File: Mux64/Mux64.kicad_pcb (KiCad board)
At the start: 4 copper layers, 198.3 x 130.3 mm, 143 parts, among them J1 QTE-020-01-X-D-A, J10 Conn_01x24, J11 Screw_Terminal_01x12, J12 Screw_Terminal_01x12, J13 Screw_Terminal_01x12, J14 Screw_Terminal_01x12, J15 Screw_Terminal_01x12, J16 Screw_Terminal_01x12, J17 Screw_Terminal_01x12, J18 Screw_Terminal_01x12, J2 QTE-020-01-X-D-A, J3 QTE-020-01-X-D-A, J4 QTE-020-01-X-D-A, J5 QTE-020-01-X-D-A, J6 QTE-020-01-X-D-A, J7 Conn_01x24, J8 Conn_01x24, J9 Conn_01x24, U1 LD1117AS12TR, U2 MAX6070

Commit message: Add files via upload
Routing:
- net GND: track 511.1 -> 513.4 mm, vias 126 -> 127
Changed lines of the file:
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@@
   (segment (start 216.18 52.43) (end 216.6 52.01) (width 0.1524) (layer "F.Cu") (net 2))
   (segment (start 214.04 50.83) (end 216.6 50.83) (width 0.1524) (layer "F.Cu") (net 2))
+  (segment (start 178.6725 60.92) (end 176.34 60.92) (width 0.25) (layer "F.Cu") (net 2))
   (segment (start 219.23 51.0525) (end 216.6125 51.0525) (width 0.1524) (layer "F.Cu") (net 2))
   (segment (start 237.86 46.83) (end 236.33 46.83) (width 0.1524) (layer "F.Cu") (net 2))
@@
   (via (at 205.27 137.25) (size 0.8) (drill 0.4) (layers "F.Cu" "B.Cu") (net 2))
   (via (at 80.37 44.92) (size 0.8) (drill 0.4) (layers "F.Cu" "B.Cu") (net 2))
+  (via (at 176.34 60.92) (size 0.8) (drill 0.4) (layers "F.Cu" "B.Cu") (net 2))
   (via (at 79.25 95.71) (size 0.8) (drill 0.4) (layers "F.Cu" "B.Cu") (net 2))
   (via (at 79.95 29.65) (size 0.8) (drill 0.4) (layers "F.Cu" "B.Cu") (net 2))

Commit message: Add files via upload
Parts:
- added H1: MountingHole, MountingHole:MountingHole_2.5mm, F.Cu at (250.7, 151.7)
- added H2: MountingHole, MountingHole:MountingHole_2.5mm, F.Cu at (85.0, 151.7)
- added H3: MountingHole, MountingHole:MountingHole_2.5mm, F.Cu at (85.0, 28.4)
- added H4: MountingHole, MountingHole:MountingHole_2.5mm, F.Cu at (250.7, 28.4)
- moved TP1 7.51 mm to (192.3, 46.9)
- moved R8 3.64 mm to (124.2, 99.0)
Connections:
- C1 pad 2: GND -> MUX64_A0
- C10 pad 2: GND -> MUX64_A0
- C11 pad 2: GND -> MUX64_A0
- C12 pad 2: GND -> MUX64_A0
- C2 pad 2: GND -> MUX64_A0
- C3 pad 2: GND -> MUX64_A0
- C4 pad 2: GND -> MUX64_A0
- C5 pad 2: GND -> MUX64_A0
- C6 pad 2: GND -> MUX64_A0
- C7 pad 2: GND -> MUX64_A0
- C8 pad 1: GND -> MUX64_A0
- C9 pad 2: GND -> MUX64_A0
- J1 pad 02: /scl -> /A_scl
- J1 pad 04: /sda -> /A_sda
- J1 pad 05: GND -> MUX64_A0
- J1 pad 06: GND -> MUX64_A0
- J1 pad 08: GND -> MUX64_A0
- J1 pad 10: GND -> MUX64_A0
- J1 pad 11: GND -> MUX64_A0
- J1 pad 12: GND -> MUX64_A0
- J1 pad 17: GND -> MUX64_A0
- J1 pad 22: GND -> MUX64_A0
- J1 pad 23: GND -> MUX64_A0
- J1 pad 24: GND -> MUX64_A0
- J1 pad 29: GND -> MUX64_A0
- J1 pad 34: GND -> MUX64_A0
- J1 pad 35: GND -> MUX64_A0
- J1 pad G1: GND -> MUX64_A0
- J1 pad G2: GND -> MUX64_A0
- J1 pad G3: GND -> MUX64_A0
- J1 pad G4: GND -> MUX64_A0
- J10 pad 1: GND -> MUX64_A0
- J10 pad 10: GND -> MUX64_A0
- J10 pad 11: GND -> MUX64_A0
- J10 pad 12: GND -> MUX64_A0
- J10 pad 2: GND -> MUX64_A0
- J10 pad 9: GND -> MUX64_A0
- J11 pad 10: GND -> MUX64_A0
- J11 pad 12: GND -> MUX64_A0
- J11 pad 2: GND -> MUX64_A0
- J11 pad 4: GND -> MUX64_A0
- J11 pad 6: GND -> MUX64_A0
- J11 pad 8: GND -> MUX64_A0
- J12 pad 10: GND -> MUX64_A0
- J12 pad 12: GND -> MUX64_A0
- J12 pad 2: GND -> MUX64_A0
- J12 pad 4: GND -> MUX64_A0
- J12 pad 6: GND -> MUX64_A0
- J12 pad 8: GND -> MUX64_A0
- J13 pad 10: GND -> MUX64_A0
- J13 pad 12: GND -> MUX64_A0
- J13 pad 2: GND -> MUX64_A0
- J13 pad 4: GND -> MUX64_A0
- J13 pad 6: GND -> MUX64_A0
- J13 pad 8: GND -> MUX64_A0
- J14 pad 10: GND -> MUX64_A0
- J14 pad 12: GND -> MUX64_A0
- J14 pad 2: GND -> MUX64_A0
- J14 pad 4: GND -> MUX64_A0
- J14 pad 6: GND -> MUX64_A0
- J14 pad 8: GND -> MUX64_A0
- J15 pad 10: GND -> MUX64_A0
- J15 pad 12: GND -> MUX64_A0
- J15 pad 2: GND -> MUX64_A0
- J15 pad 4: GND -> MUX64_A0
- J15 pad 6: GND -> MUX64_A0
- J15 pad 8: GND -> MUX64_A0
- J16 pad 10: GND -> MUX64_A0
- J16 pad 12: GND -> MUX64_A0
- J16 pad 2: GND -> MUX64_A0
- J16 pad 4: GND -> MUX64_A0
- J16 pad 6: GND -> MUX64_A0
- J16 pad 8: GND -> MUX64_A0
- J17 pad 10: GND -> MUX64_A0
- J17 pad 12: GND -> MUX64_A0
- J17 pad 2: GND -> MUX64_A0
- J17 pad 4: GND -> MUX64_A0
- J17 pad 6: GND -> MUX64_A0
- J17 pad 8: GND -> MUX64_A0
- J18 pad 10: GND -> MUX64_A0
- J18 pad 12: GND -> MUX64_A0
- J18 pad 2: GND -> MUX64_A0
- J18 pad 4: GND -> MUX64_A0
- J18 pad 6: GND -> MUX64_A0
- J18 pad 8: GND -> MUX64_A0
- J2 pad 02: /scl -> /C_scl
- J2 pad 04: /sda -> /C_sda
- J2 pad 05: GND -> MUX64_A0
- J2 pad 06: GND -> MUX64_A0
- J2 pad 08: GND -> MUX64_A0
- J2 pad 10: GND -> MUX64_A0
- J2 pad 11: GND -> MUX64_A0
- J2 pad 12: GND -> MUX64_A0
- J2 pad 17: GND -> MUX64_A0
- J2 pad 22: GND -> MUX64_A0
- J2 pad 23: GND -> MUX64_A0
- J2 pad 24: GND -> MUX64_A0
- J2 pad 29: GND -> MUX64_A0
- J2 pad 34: GND -> MUX64_A0
- J2 pad 35: GND -> MUX64_A0
- J2 pad G1: GND -> MUX64_A0
- J2 pad G2: GND -> MUX64_A0
- J2 pad G3: GND -> MUX64_A0
- J2 pad G4: GND -> MUX64_A0
- J3 pad 06: GND -> MUX64_A0
- J3 pad 07: GND -> MUX64_A0
- J3 pad 12: GND -> MUX64_A0
- J3 pad 17: GND -> MUX64_A0
- J3 pad 18: GND -> MUX64_A0
- J3 pad 19: GND -> MUX64_A0
- J3 pad 24: GND -> MUX64_A0
- J3 pad 29: GND -> MUX64_A0
- J3 pad 30: GND -> MUX64_A0
- J3 pad 31: GND -> MUX64_A0
- J3 pad 33: GND -> MUX64_A0
- J3 pad 36: GND -> MUX64_A0
- J3 pad G1: GND -> MUX64_A0
- J3 pad G2: GND -> MUX64_A0
- J3 pad G3: GND -> MUX64_A0
- J3 pad G4: GND -> MUX64_A0
- J4 pad 06: GND -> MUX64_A0
- J4 pad 07: GND -> MUX64_A0
- J4 pad 12: GND -> MUX64_A0
- J4 pad 17: GND -> MUX64_A0
- J4 pad 18: GND -> MUX64_A0
- J4 pad 19: GND -> MUX64_A0
- J4 pad 24: GND -> MUX64_A0
- J4 pad 29: GND -> MUX64_A0
- J4 pad 30: GND -> MUX64_A0
- J4 pad 31: GND -> MUX64_A0
- J4 pad 33: GND -> MUX64_A0
- J4 pad 36: GND -> MUX64_A0
- J4 pad G1: GND -> MUX64_A0
- J4 pad G2: GND -> MUX64_A0
- J4 pad G3: GND -> MUX64_A0
- J4 pad G4: GND -> MUX64_A0
- J5 pad 05: GND -> MUX64_A0
- J5 pad 06: GND -> MUX64_A0
- J5 pad 08: GND -> MUX64_A0
- J5 pad 10: GND -> MUX64_A0
- J5 pad 11: GND -> MUX64_A0
- J5 pad 12: GND -> MUX64_A0
- J5 pad 17: GND -> MUX64_A0
- J5 pad 22: GND -> MUX64_A0
- J5 pad 23: GND -> MUX64_A0
- J5 pad 24: GND -> MUX64_A0
- J5 pad 29: GND -> MUX64_A0
- J5 pad 34: GND -> MUX64_A0
- J5 pad 35: GND -> MUX64_A0
- J5 pad G1: GND -> MUX64_A0
- J5 pad G2: GND -> MUX64_A0
- J5 pad G3: GND -> MUX64_A0
- J5 pad G4: GND -> MUX64_A0
- J6 pad 06: GND -> MUX64_A0
- J6 pad 07: GND -> MUX64_A0
- J6 pad 12: GND -> MUX64_A0
- J6 pad 17: GND -> MUX64_A0
- J6 pad 18: GND -> MUX64_A0
- J6 pad 19: GND -> MUX64_A0
- J6 pad 24: GND -> MUX64_A0
- J6 pad 29: GND -> MUX64_A0
- J6 pad 30: GND -> MUX64_A0
- J6 pad 31: GND -> MUX64_A0
- J6 pad 33: GND -> MUX64_A0
- J6 pad 36: GND -> MUX64_A0
- J6 pad G1: GND -> MUX64_A0
- J6 pad G2: GND -> MUX64_A0
- J6 pad G3: GND -> MUX64_A0
- J6 pad G4: GND -> MUX64_A0
- J7 pad 23: GND -> MUX64_A0
- J7 pad 24: GND -> MUX64_A0
- J8 pad 23: GND -> MUX64_A0
- J8 pad 24: GND -> MUX64_A0
- J9 pad 23: GND -> MUX64_A0
- J9 pad 24: GND -> MUX64_A0
- R1 pad 1: GND -> MUX64_A0
- R10 pad 1: GND -> MUX64_A0
- R11 pad 1: GND -> MUX64_A0
- R12 pad 1: GND -> MUX64_A0
- R13 pad 1: GND -> MUX64_A0
- R14 pad 1: GND -> MUX64_A0
- R15 pad 1: GND -> MUX64_A0
- R16 pad 1: GND -> MUX64_A0
- R17 pad 1: GND -> MUX64_A0
- R18 pad 1: GND -> MUX64_A0
- R19 pad 1: GND -> MUX64_A0
- R2 pad 1: GND -> MUX64_A0
- R20 pad 1: GND -> MUX64_A0
- R3 pad 1: GND -> MUX64_A0
- R39 pad 1: GND -> MUX64_A0
- R40 pad 1: GND -> MUX64_A0
- R41 pad 1: GND -> MUX64_A0
- R42 pad 1: GND -> MUX64_A0
- R43 pad 1: GND -> MUX64_A0
- R44 pad 1: GND -> MUX64_A0
- R45 pad 1: GND -> MUX64_A0
- R46 pad 1: GND -> MUX64_A0
- R47 pad 1: GND -> MUX64_A0
- R48 pad 1: GND -> MUX64_A0
- R49 pad 1: GND -> MUX64_A0
- R50 pad 1: GND -> MUX64_A0
- R6 pad 2: GND -> MUX64_A0
- R63 pad 1: GND -> MUX64_A0
- R64 pad 1: GND -> MUX64_A0
- R65 pad 1: GND -> MUX64_A0
- R66 pad 1: GND -> MUX64_A0
- R67 pad 1: GND -> MUX64_A0
- R68 pad 1: GND -> MUX64_A0
- R69 pad 1: GND -> MUX64_A0
- R7 pad 2: GND -> MUX64_A0
- R70 pad 1: GND -> MUX64_A0
- R71 pad 1: GND -> MUX64_A0
- R72 pad 1: GND -> MUX64_A0
- R73 pad 1: GND -> MUX64_A0
- R74 pad 1: GND -> MUX64_A0
- R87 pad 1: GND -> MUX64_A0
- R88 pad 1: GND -> MUX64_A0
- R89 pad 1: GND -> MUX64_A0
- R9 pad 1: GND -> MUX64_A0
- R90 pad 1: GND -> MUX64_A0
- R91 pad 1: GND -> MUX64_A0
- R92 pad 1: GND -> MUX64_A0
- R93 pad 1: GND -> MUX64_A0
- R94 pad 1: GND -> MUX64_A0
- R95 pad 1: GND -> MUX64_A0
- R96 pad 1: GND -> MUX64_A0
- R97 pad 1: GND -> MUX64_A0
- R98 pad 1: GND -> MUX64_A0
- U1 pad 1: GND -> MUX64_A0
- U2 pad 2: GND -> MUX64_A0
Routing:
- net GND: track 513.4 -> 4.04 mm, vias 127 -> 1
- net MUX64_A0: track 977.2 -> 602.3 mm, vias 6 -> 128
- net MUX64_A30: track 116.4 -> 120.3 mm
- net MUX64_A31: track 111.6 -> 114.9 mm
- net MUX64_A27: track 127.4 -> 130.1 mm
- net MUX64_A32: track 112.8 -> 115.3 mm
- net MUX64_A35: track 167.3 -> 169.5 mm
- net MUX64_A33: track 110.6 -> 112.2 mm
- net MUX64_A37: track 176.7 -> 178.3 mm
- net B_a4: track 140.0 -> 141.5 mm
- net MUX64_A29: track 115.5 -> 117.0 mm
- net MUX64_A41: track 209.6 -> 208.5 mm
- net MUX64_A38: track 188.3 -> 189.2 mm
- net MUX64_A40: track 206.5 -> 205.8 mm
- net MUX64_A25: track 131.0 -> 130.5 mm
- added copper zone on In1.Cu, net MUX64_A0
- added copper zone on In2.Cu, net MUX64_A0
- removed copper zone on In1.Cu, net GND
- removed copper zone on In2.Cu, net GND
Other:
- board text added: "(\__/) ( •-•) / >"
- board text added: "Boston University"
- board text added: "~1/1250 Vin"
- board text added: "~1/2 Vin"
- board text added: "~1/4 Vin"
- board text added: "~2/25 Vin"

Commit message: Final revision
Fixed high voltage spacial issue and distributed traces to have less density on the bottom of the board
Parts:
- removed J15: Screw_Terminal_01x12, TerminalBlock_Phoenix:TerminalBlock_Phoenix_MPT-0,5-12-2.54_1x12_P2.54mm_Horizontal
- removed R24, R25, R26, R33, R34, R35, R36, R37, R38: 50Mohm, Resistor_SMD:R_1206_3216Metric
- removed R63, R65, R66, R67, R68, R69, R75, R76, R77, R78, R79, R80: 82Kohm, Resistor_SMD:R_0805_2012Metric
- J12: value Screw_Terminal_01x12 -> Screw_Terminal_01x06; footprint TerminalBlock_Phoenix:TerminalBlock_Phoenix_MPT-0,5-12-2.54_1x12_P2.54mm_Horizontal -> TerminalBlock_RND:TerminalBlock_RND_205-00071_1x06_P7.50mm_Horizontal
- R11, R12, R13, R14: value 82Kohm -> 50Mohm; footprint Resistor_SMD:R_0805_2012Metric -> Resistor_SMD:R_1206_3216Metric
- R23: value 50Mohm -> 1Kohm; footprint Resistor_SMD:R_1206_3216Metric -> Resistor_SMD:R_0805_2012Metric
- R8: value 0ohm -> 82Kohm
- moved R10 69.8 mm to (124.6, 77.7)
- moved R22 69.6 mm to (108.0, 77.7)
- moved R9 60.1 mm to (124.6, 92.6)
- moved R21 59.8 mm to (108.0, 92.6)
- moved R23 56.2 mm to (141.4, 94.7)
- moved R13 54.4 mm to (116.4, 77.7)
- moved J12 45.0 mm to (97.9, 107.6)
- moved R57 44.8 mm to (102.7, 152.6)
- moved R58 44.8 mm to (102.7, 147.5)
- moved R59 44.8 mm to (102.7, 142.4)
- moved R61 44.8 mm to (102.7, 132.2)
- moved R62 44.8 mm to (102.7, 127.2)
- moved J14 44.8 mm to (92.9, 152.6)
- moved R60 44.8 mm to (102.7, 137.3)
- moved R40 44.6 mm to (110.2, 152.6)
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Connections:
- C1 pad 2: MUX64_A0 -> MUX64_A42
- C10 pad 2: MUX64_A0 -> MUX64_A42
- C11 pad 2: MUX64_A0 -> MUX64_A42
- C12 pad 2: MUX64_A0 -> MUX64_A42
- C2 pad 2: MUX64_A0 -> MUX64_A42
- C3 pad 2: MUX64_A0 -> MUX64_A42
- C4 pad 2: MUX64_A0 -> MUX64_A42
- C5 pad 2: MUX64_A0 -> MUX64_A42
- C6 pad 2: MUX64_A0 -> MUX64_A42
- C7 pad 2: MUX64_A0 -> MUX64_A42
- C8 pad 1: MUX64_A0 -> MUX64_A42
- C9 pad 2: MUX64_A0 -> MUX64_A42
- J1 pad 05: MUX64_A0 -> MUX64_A42
- J1 pad 06: MUX64_A0 -> MUX64_A42
- J1 pad 08: MUX64_A0 -> MUX64_A42
- J1 pad 10: MUX64_A0 -> MUX64_A42
- J1 pad 11: MUX64_A0 -> MUX64_A42
- J1 pad 12: MUX64_A0 -> MUX64_A42
- J1 pad 17: MUX64_A0 -> MUX64_A42
- J1 pad 22: MUX64_A0 -> MUX64_A42
- J1 pad 23: MUX64_A0 -> MUX64_A42
- J1 pad 24: MUX64_A0 -> MUX64_A42
- J1 pad 29: MUX64_A0 -> MUX64_A42
- J1 pad 34: MUX64_A0 -> MUX64_A42
- J1 pad 35: MUX64_A0 -> MUX64_A42
- J1 pad G1: MUX64_A0 -> MUX64_A42
- J1 pad G2: MUX64_A0 -> MUX64_A42
- J1 pad G3: MUX64_A0 -> MUX64_A42
- J1 pad G4: MUX64_A0 -> MUX64_A42
- J10 pad 1: MUX64_A0 -> MUX64_A42
- J10 pad 10: MUX64_A0 -> MUX64_A42
- J10 pad 11: MUX64_A0 -> MUX64_A42
- J10 pad 12: MUX64_A0 -> MUX64_A42
- J10 pad 15: MUX64_A0 -> MUX64_A42
- J10 pad 16: MUX64_A0 -> MUX64_A42
- J10 pad 17: MUX64_A0 -> MUX64_A42
- J10 pad 2: MUX64_A0 -> MUX64_A42
- J10 pad 9: MUX64_A0 -> MUX64_A42
- J11 pad 10: MUX64_A0 -> MUX64_A42
- J11 pad 12: MUX64_A0 -> MUX64_A42
- J11 pad 2: MUX64_A0 -> MUX64_A42
- J11 pad 4: MUX64_A0 -> MUX64_A42
- J11 pad 6: MUX64_A0 -> MUX64_A42
- J11 pad 8: MUX64_A0 -> MUX64_A42
- J12 pad 2: MUX64_A0 -> MUX64_A42
- J12 pad 4: MUX64_A0 -> MUX64_A42
- J12 pad 6: MUX64_A0 -> MUX64_A42
- J13 pad 10: MUX64_A0 -> MUX64_A42
- J13 pad 12: MUX64_A0 -> MUX64_A42
- J13 pad 2: MUX64_A0 -> MUX64_A42
- J13 pad 4: MUX64_A0 -> MUX64_A42
- J13 pad 6: MUX64_A0 -> MUX64_A42
- J13 pad 8: MUX64_A0 -> MUX64_A42
- J14 pad 10: MUX64_A0 -> MUX64_A42
- J14 pad 12: MUX64_A0 -> MUX64_A42
- J14 pad 2: MUX64_A0 -> MUX64_A42
- J14 pad 4: MUX64_A0 -> MUX64_A42
- J14 pad 6: MUX64_A0 -> MUX64_A42
- J14 pad 8: MUX64_A0 -> MUX64_A42
- J16 pad 10: MUX64_A0 -> MUX64_A42
- J16 pad 12: MUX64_A0 -> MUX64_A42
- J16 pad 2: MUX64_A0 -> MUX64_A42
- J16 pad 4: MUX64_A0 -> MUX64_A42
- J16 pad 6: MUX64_A0 -> MUX64_A42
- J16 pad 8: MUX64_A0 -> MUX64_A42
- J17 pad 10: MUX64_A0 -> MUX64_A42
- J17 pad 12: MUX64_A0 -> MUX64_A42
- J17 pad 2: MUX64_A0 -> MUX64_A42
- J17 pad 4: MUX64_A0 -> MUX64_A42
- J17 pad 6: MUX64_A0 -> MUX64_A42
- J17 pad 8: MUX64_A0 -> MUX64_A42
- J18 pad 10: MUX64_A0 -> MUX64_A42
- J18 pad 12: MUX64_A0 -> MUX64_A42
- J18 pad 2: MUX64_A0 -> MUX64_A42
- J18 pad 4: MUX64_A0 -> MUX64_A42
- J18 pad 6: MUX64_A0 -> MUX64_A42
- J18 pad 8: MUX64_A0 -> MUX64_A42
- J2 pad 05: MUX64_A0 -> MUX64_A42
- J2 pad 06: MUX64_A0 -> MUX64_A42
- J2 pad 08: MUX64_A0 -> MUX64_A42
- J2 pad 10: MUX64_A0 -> MUX64_A42
- J2 pad 11: MUX64_A0 -> MUX64_A42
- J2 pad 12: MUX64_A0 -> MUX64_A42
- J2 pad 17: MUX64_A0 -> MUX64_A42
- J2 pad 22: MUX64_A0 -> MUX64_A42
- J2 pad 23: MUX64_A0 -> MUX64_A42
- J2 pad 24: MUX64_A0 -> MUX64_A42
- J2 pad 29: MUX64_A0 -> MUX64_A42
- J2 pad 34: MUX64_A0 -> MUX64_A42
- J2 pad 35: MUX64_A0 -> MUX64_A42
- J2 pad G1: MUX64_A0 -> MUX64_A42
- J2 pad G2: MUX64_A0 -> MUX64_A42
- J2 pad G3: MUX64_A0 -> MUX64_A42
- J2 pad G4: MUX64_A0 -> MUX64_A42
- J3 pad 06: MUX64_A0 -> MUX64_A42
- J3 pad 07: MUX64_A0 -> MUX64_A42
- J3 pad 12: MUX64_A0 -> MUX64_A42
- J3 pad 17: MUX64_A0 -> MUX64_A42
- J3 pad 18: MUX64_A0 -> MUX64_A42
- J3 pad 19: MUX64_A0 -> MUX64_A42
- J3 pad 24: MUX64_A0 -> MUX64_A42
- J3 pad 29: MUX64_A0 -> MUX64_A42
- J3 pad 30: MUX64_A0 -> MUX64_A42
- J3 pad 31: MUX64_A0 -> MUX64_A42
- J3 pad 33: MUX64_A0 -> MUX64_A42
- J3 pad 36: MUX64_A0 -> MUX64_A42
- J3 pad G1: MUX64_A0 -> MUX64_A42
- J3 pad G2: MUX64_A0 -> MUX64_A42
- J3 pad G3: MUX64_A0 -> MUX64_A42
- J3 pad G4: MUX64_A0 -> MUX64_A42
- J4 pad 06: MUX64_A0 -> MUX64_A42
- J4 pad 07: MUX64_A0 -> MUX64_A42
- J4 pad 12: MUX64_A0 -> MUX64_A42
- J4 pad 17: MUX64_A0 -> MUX64_A42
- J4 pad 18: MUX64_A0 -> MUX64_A42
- J4 pad 19: MUX64_A0 -> MUX64_A42
- J4 pad 24: MUX64_A0 -> MUX64_A42
- J4 pad 29: MUX64_A0 -> MUX64_A42
- J4 pad 30: MUX64_A0 -> MUX64_A42
- J4 pad 31: MUX64_A0 -> MUX64_A42
- J4 pad 33: MUX64_A0 -> MUX64_A42
- J4 pad 36: MUX64_A0 -> MUX64_A42
- J4 pad G1: MUX64_A0 -> MUX64_A42
- J4 pad G2: MUX64_A0 -> MUX64_A42
- J4 pad G3: MUX64_A0 -> MUX64_A42
- J4 pad G4: MUX64_A0 -> MUX64_A42
- J5 pad 05: MUX64_A0 -> MUX64_A42
- J5 pad 06: MUX64_A0 -> MUX64_A42
- J5 pad 08: MUX64_A0 -> MUX64_A42
- J5 pad 10: MUX64_A0 -> MUX64_A42
- J5 pad 11: MUX64_A0 -> MUX64_A42
- J5 pad 12: MUX64_A0 -> MUX64_A42
- J5 pad 17: MUX64_A0 -> MUX64_A42
- J5 pad 22: MUX64_A0 -> MUX64_A42
- J5 pad 23: MUX64_A0 -> MUX64_A42
- J5 pad 24: MUX64_A0 -> MUX64_A42
- J5 pad 29: MUX64_A0 -> MUX64_A42
- J5 pad 34: MUX64_A0 -> MUX64_A42
- J5 pad 35: MUX64_A0 -> MUX64_A42
- J5 pad G1: MUX64_A0 -> MUX64_A42
- J5 pad G2: MUX64_A0 -> MUX64_A42
- J5 pad G3: MUX64_A0 -> MUX64_A42
- J5 pad G4: MUX64_A0 -> MUX64_A42
- J6 pad 06: MUX64_A0 -> MUX64_A42
- J6 pad 07: MUX64_A0 -> MUX64_A42
- J6 pad 12: MUX64_A0 -> MUX64_A42
- J6 pad 17: MUX64_A0 -> MUX64_A42
- J6 pad 18: MUX64_A0 -> MUX64_A42
- J6 pad 19: MUX64_A0 -> MUX64_A42
- J6 pad 24: MUX64_A0 -> MUX64_A42
- J6 pad 29: MUX64_A0 -> MUX64_A42
- J6 pad 30: MUX64_A0 -> MUX64_A42
- J6 pad 31: MUX64_A0 -> MUX64_A42
- J6 pad 33: MUX64_A0 -> MUX64_A42
- J6 pad 36: MUX64_A0 -> MUX64_A42
- J6 pad G1: MUX64_A0 -> MUX64_A42
- J6 pad G2: MUX64_A0 -> MUX64_A42
- J6 pad G3: MUX64_A0 -> MUX64_A42
- J6 pad G4: MUX64_A0 -> MUX64_A42
- J7 pad 19: MUX64_A12 -> MUX64_A42
- J7 pad 20: MUX64_A11 -> MUX64_A42
- J7 pad 22: MUX64_A13 -> MUX64_A42
- J7 pad 23: MUX64_A0 -> MUX64_A42
- J7 pad 24: MUX64_A0 -> MUX64_A42
- J8 pad 15: MUX64_A0 -> MUX64_A42
- J8 pad 16: MUX64_A27 -> MUX64_A42
- J8 pad 2: MUX64_A0 -> MUX64_A42
- J8 pad 23: MUX64_A0 -> MUX64_A42
- J8 pad 24: MUX64_A0 -> MUX64_A42
- J9 pad 11: MUX64_A0 -> MUX64_A42
- J9 pad 12: MUX64_A43 -> MUX64_A42
- J9 pad 13: MUX64_A0 -> MUX64_A42
- J9 pad 14: MUX64_A45 -> MUX64_A42
- J9 pad 15: MUX64_A0 -> MUX64_A42
- J9 pad 16: MUX64_A47 -> MUX64_A42
- J9 pad 17: MUX64_A0 -> MUX64_A42
- J9 pad 18: MUX64_A49 -> MUX64_A42
- J9 pad 19: MUX64_A0 -> MUX64_A42
- J9 pad 2: MUX64_A0 -> MUX64_A34
- J9 pad 20: MUX64_A51 -> MUX64_A42
- J9 pad 22: MUX64_A53 -> MUX64_A42
- J9 pad 23: MUX64_A0 -> MUX64_A42
- J9 pad 24: MUX64_A0 -> MUX64_A42
- J9 pad 3: MUX64_A0 -> MUX64_A42
- J9 pad 9: MUX64_A0 -> MUX64_A42
- R1 pad 1: MUX64_A0 -> MUX64_A42
- R10 pad 1: MUX64_A0 -> MUX64_A42
- R10 pad 2: MUX64_A51 -> MUX64_A8
- R105 pad 1: MUX64_A7 -> MUX64_A16
- R106 pad 1: MUX64_A6 -> MUX64_A15
- R107 pad 1: MUX64_A5 -> MUX64_A18
- R108 pad 1: MUX64_A4 -> MUX64_A17
- R109 pad 1: MUX64_A3 -> MUX64_A20
- R11 pad 1: MUX64_A0 -> MUX64_A10
- R11 pad 2: MUX64_A49 -> Net-(R11-Pad2)
- R110 pad 1: MUX64_A2 -> MUX64_A19
- R12 pad 1: MUX64_A0 -> MUX64_A9
- R12 pad 2: MUX64_A47 -> Net-(R12-Pad2)
- R13 pad 1: MUX64_A0 -> MUX64_A8
- R13 pad 2: MUX64_A45 -> Net-(R13-Pad2)
- R14 pad 1: MUX64_A0 -> Net-(R11-Pad2)
- R14 pad 2: MUX64_A43 -> Net-(J12-Pad1)
- R15 pad 1: MUX64_A0 -> MUX64_A42
- R15 pad 2: MUX64_A41 -> MUX64_A35
- R16 pad 1: MUX64_A0 -> MUX64_A42
- R16 pad 2: MUX64_A40 -> MUX64_A38
- R17 pad 1: MUX64_A0 -> MUX64_A42
- R17 pad 2: MUX64_A39 -> MUX64_A37
- R18 pad 1: MUX64_A0 -> MUX64_A42
- R18 pad 2: MUX64_A38 -> MUX64_A40
- R19 pad 1: MUX64_A0 -> MUX64_A42
- R19 pad 2: MUX64_A37 -> MUX64_A39
- R2 pad 1: MUX64_A0 -> MUX64_A42
- R20 pad 1: MUX64_A0 -> MUX64_A42
- R20 pad 2: MUX64_A35 -> MUX64_A41
- R21 pad 1: MUX64_A53 -> Net-(R12-Pad2)
- R21 pad 2: Net-(R21-Pad2) -> Net-(J12-Pad3)
- R22 pad 1: MUX64_A51 -> Net-(R13-Pad2)
- R22 pad 2: Net-(R22-Pad2) -> Net-(J12-Pad5)
- R23 pad 1: MUX64_A49 -> MUX64_A0
- R23 pad 2: Net-(R23-Pad2) -> MUX64_A42
- R27 pad 1: MUX64_A41 -> MUX64_A35
- R28 pad 1: MUX64_A40 -> MUX64_A38
- R29 pad 1: MUX64_A39 -> MUX64_A37
- R3 pad 1: MUX64_A0 -> MUX64_A42
- R30 pad 1: MUX64_A38 -> MUX64_A40
- R31 pad 1: MUX64_A37 -> MUX64_A39
- R32 pad 1: MUX64_A35 -> MUX64_A41
- R39 pad 1: MUX64_A0 -> MUX64_A42
- R40 pad 1: MUX64_A0 -> MUX64_A42
- R40 pad 2: MUX64_A33 -> MUX64_A34
- R41 pad 1: MUX64_A0 -> MUX64_A42
- R42 pad 1: MUX64_A0 -> MUX64_A42
- R43 pad 1: MUX64_A0 -> MUX64_A42
- R44 pad 1: MUX64_A0 -> MUX64_A42
- R45 pad 1: MUX64_A0 -> MUX64_A42
- R46 pad 1: MUX64_A0 -> MUX64_A42
- R46 pad 2: MUX64_A32 -> MUX64_A33
- R47 pad 1: MUX64_A0 -> MUX64_A42
- R47 pad 2: MUX64_A31 -> MUX64_A32
- R48 pad 1: MUX64_A0 -> MUX64_A42
- R48 pad 2: MUX64_A30 -> MUX64_A31
- R49 pad 1: MUX64_A0 -> MUX64_A42
- R49 pad 2: MUX64_A29 -> MUX64_A30
- R50 pad 1: MUX64_A0 -> MUX64_A42
- R50 pad 2: MUX64_A27 -> MUX64_A29
- R57 pad 1: MUX64_A33 -> MUX64_A34
- R58 pad 1: MUX64_A32 -> MUX64_A33
- R59 pad 1: MUX64_A31 -> MUX64_A32
- R6 pad 2: MUX64_A0 -> MUX64_A42
- R60 pad 1: MUX64_A30 -> MUX64_A31
- R61 pad 1: MUX64_A29 -> MUX64_A30
- R62 pad 1: MUX64_A27 -> MUX64_A29
- R64 pad 1: MUX64_A0 -> MUX64_A42
- R64 pad 2: MUX64_A13 -> MUX64_A7
- R7 pad 2: MUX64_A0 -> MUX64_A42
- R70 pad 1: MUX64_A0 -> MUX64_A42
- R70 pad 2: MUX64_A12 -> MUX64_A6
- R71 pad 1: MUX64_A0 -> MUX64_A42
- R71 pad 2: MUX64_A11 -> MUX64_A5
- R72 pad 1: MUX64_A0 -> MUX64_A42
- R72 pad 2: MUX64_A10 -> MUX64_A4
- R73 pad 1: MUX64_A0 -> MUX64_A42
- R73 pad 2: MUX64_A9 -> MUX64_A3
- R74 pad 1: MUX64_A0 -> MUX64_A42
- R74 pad 2: MUX64_A8 -> MUX64_A2
- R8 pad 1: GND -> MUX64_A42
- R8 pad 2: MUX64_A0 -> MUX64_A10
- R81 pad 1: MUX64_A13 -> MUX64_A7
- R82 pad 1: MUX64_A12 -> MUX64_A6
- R83 pad 1: MUX64_A11 -> MUX64_A5
- R84 pad 1: MUX64_A10 -> MUX64_A4
- R85 pad 1: MUX64_A9 -> MUX64_A3
- R86 pad 1: MUX64_A8 -> MUX64_A2
- R87 pad 1: MUX64_A0 -> MUX64_A42
- R88 pad 1: MUX64_A0 -> MUX64_A42
- R88 pad 2: MUX64_A7 -> MUX64_A16
- R89 pad 1: MUX64_A0 -> MUX64_A42
- R9 pad 1: MUX64_A0 -> MUX64_A42
- R9 pad 2: MUX64_A53 -> MUX64_A9
- R90 pad 1: MUX64_A0 -> MUX64_A42
- R91 pad 1: MUX64_A0 -> MUX64_A42
- R92 pad 1: MUX64_A0 -> MUX64_A42
- R93 pad 1: MUX64_A0 -> MUX64_A42
- R94 pad 1: MUX64_A0 -> MUX64_A42
- R94 pad 2: MUX64_A6 -> MUX64_A15
- R95 pad 1: MUX64_A0 -> MUX64_A42
- R95 pad 2: MUX64_A5 -> MUX64_A18
- R96 pad 1: MUX64_A0 -> MUX64_A42
- R96 pad 2: MUX64_A4 -> MUX64_A17
- R97 pad 1: MUX64_A0 -> MUX64_A42
- R97 pad 2: MUX64_A3 -> MUX64_A20
- R98 pad 1: MUX64_A0 -> MUX64_A42
- R98 pad 2: MUX64_A2 -> MUX64_A19
- U1 pad 1: MUX64_A0 -> MUX64_A42
- U2 pad 2: MUX64_A0 -> MUX64_A42
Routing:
- net MUX64_A0: track 602.3 -> 47.5 mm, vias 128 -> 0
- net MUX64_A42: track 0.00 -> 494.2 mm, vias 0 -> 118
- net MUX64_A53: track 149.2 -> 0.00 mm
- net MUX64_A51: track 148.0 -> 0.00 mm
- net MUX64_A49: track 144.7 -> 0.00 mm
- net MUX64_A47: track 143.0 -> 0.00 mm
- net MUX64_A45: track 143.0 -> 0.00 mm
- net MUX64_A43: track 141.2 -> 0.00 mm
- net MUX64_A27: track 130.1 -> 0.00 mm, vias 1 -> 0
- net MUX64_A11: track 119.9 -> 0.00 mm, vias 1 -> 0
- net MUX64_A12: track 118.7 -> 0.00 mm, vias 1 -> 0
- net MUX64_A13: track 110.8 -> 0.00 mm, vias 1 -> 0
- net MUX64_A34: track 0.00 -> 100.6 mm
- net MUX64_A19: track 112.8 -> 205.5 mm
- net MUX64_A20: track 105.9 -> 193.8 mm
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- added copper zone on In1.Cu, net MUX64_A42
- added copper zone on In2.Cu, net MUX64_A42
- removed copper zone on In1.Cu, net MUX64_A0
- removed copper zone on In2.Cu, net MUX64_A0

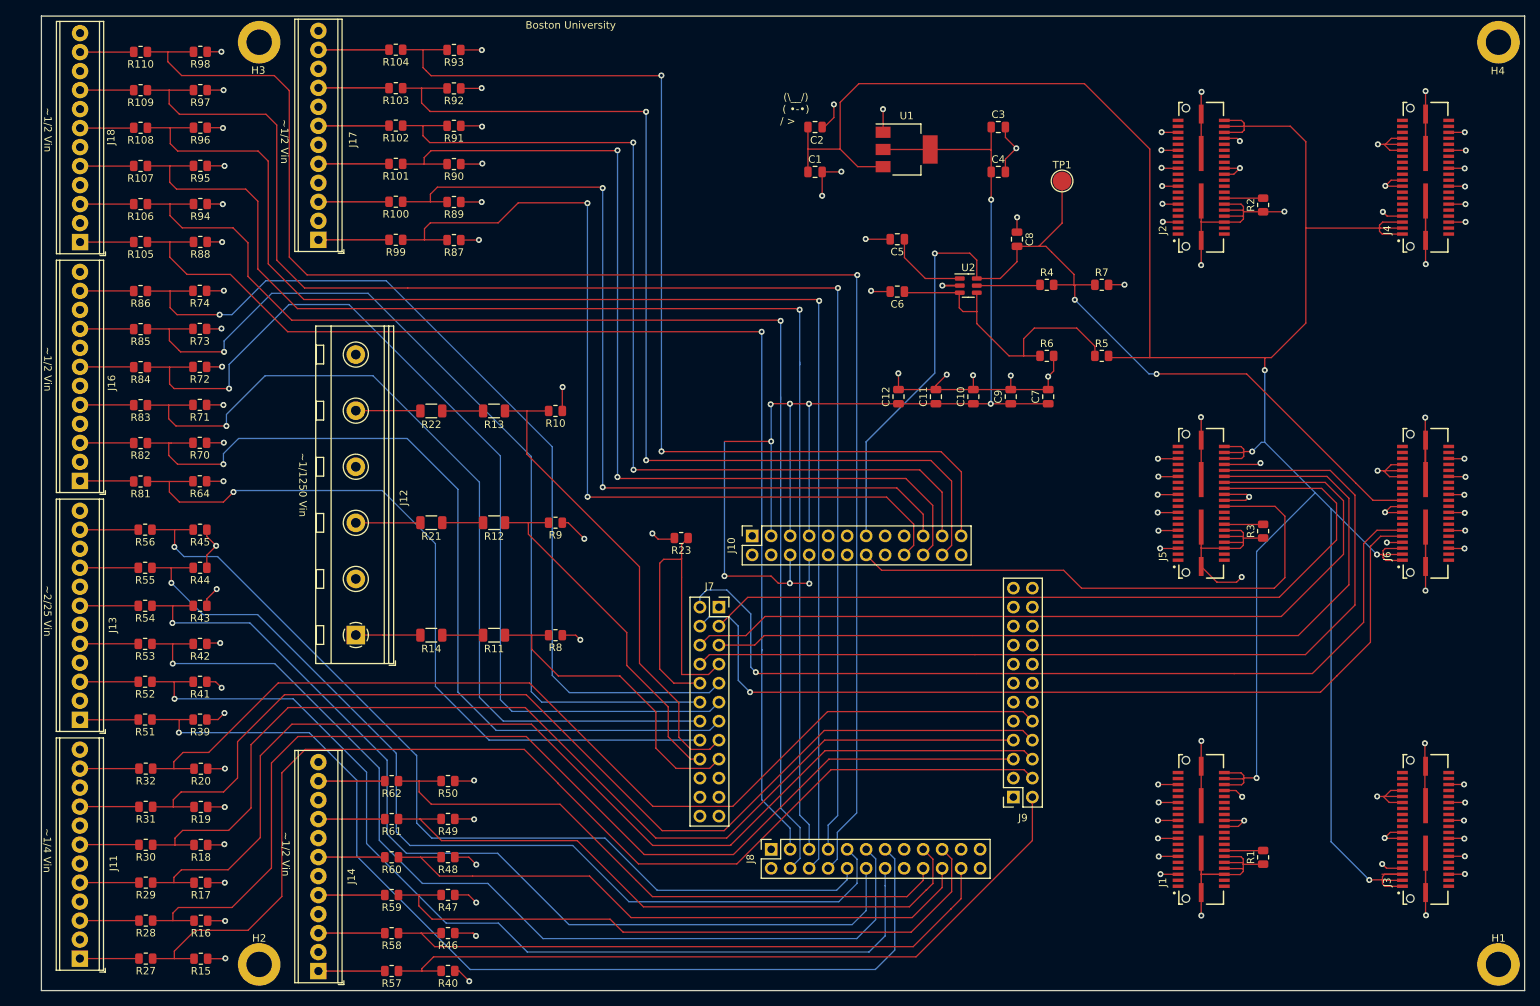
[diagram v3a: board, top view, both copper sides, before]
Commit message: Added +/-
Made silkscreen more visible
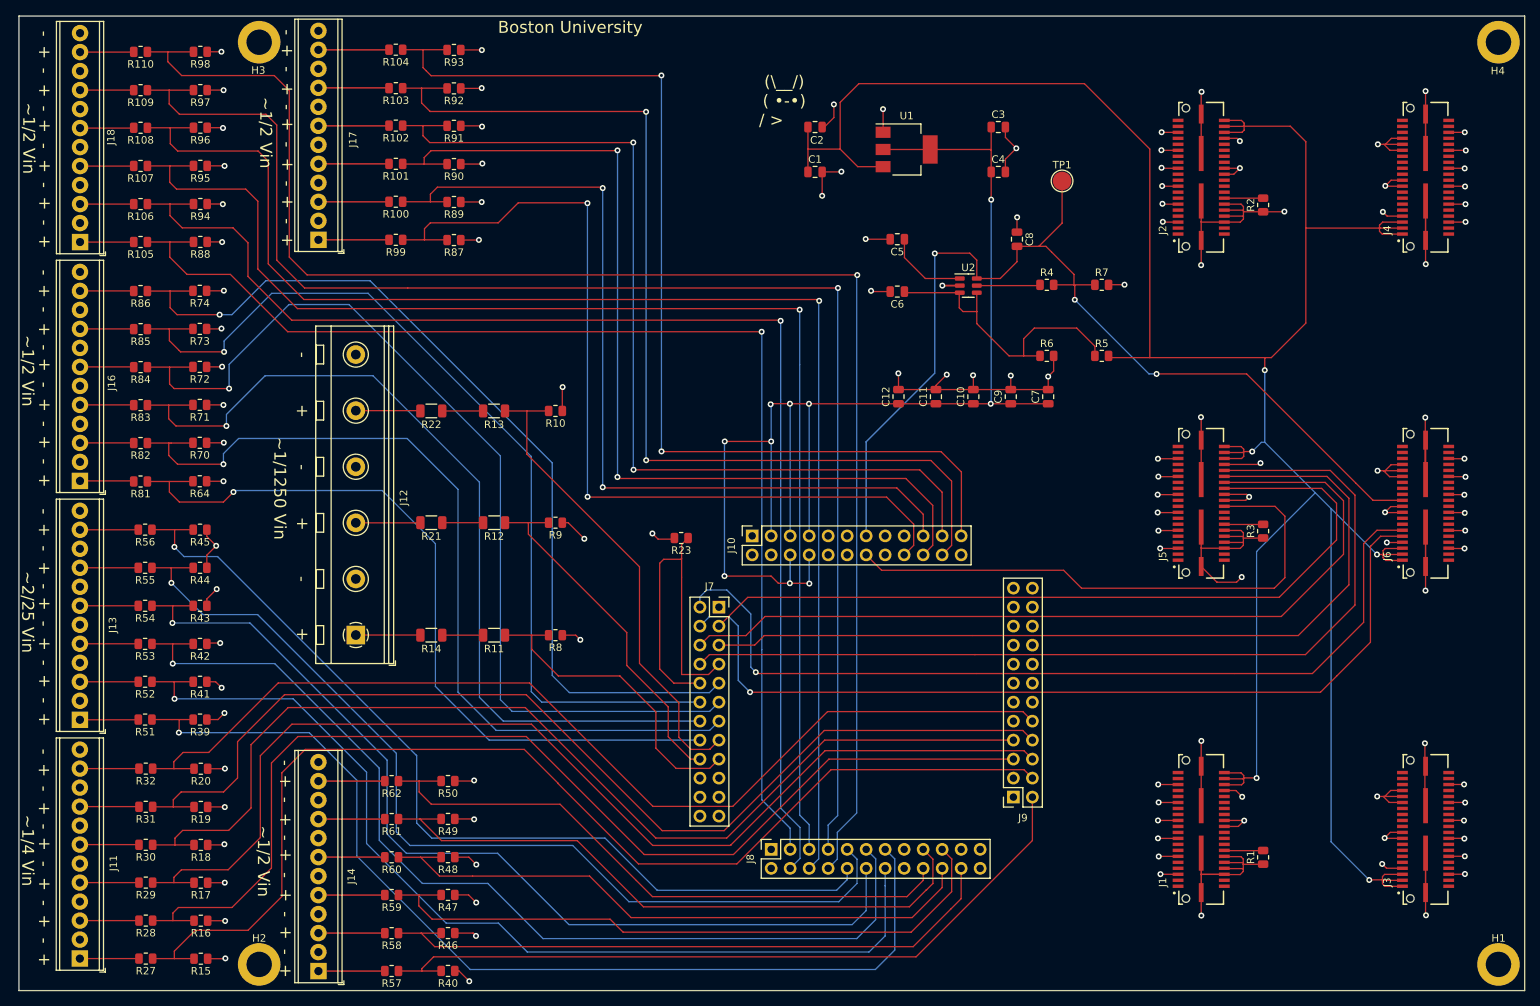
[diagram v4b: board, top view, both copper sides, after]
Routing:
- net LV_RB: track 361.5 -> 358.9 mm
- net MUX64_A2: track 125.2 -> 124.0 mm
- net MUX64_A18: track 178.1 -> 177.6 mm
- net 1.2V: vias 9 -> 10
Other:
- board size 198.3 x 130.3 mm -> 201.3 x 130.3 mm
- board text added: "+"
- board text added: "-"
